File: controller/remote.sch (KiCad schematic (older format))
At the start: 24 parts, among them J1 Conn_01x03, J2 Conn_01x02, J3 Conn_01x07, J4 Conn_01x03, J5 Conn_01x03, J6 Conn_01x02, J7 Conn_01x03, U3 Arduino_Nano_v3.x, U4 AP1117, U5 nRF24L01+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

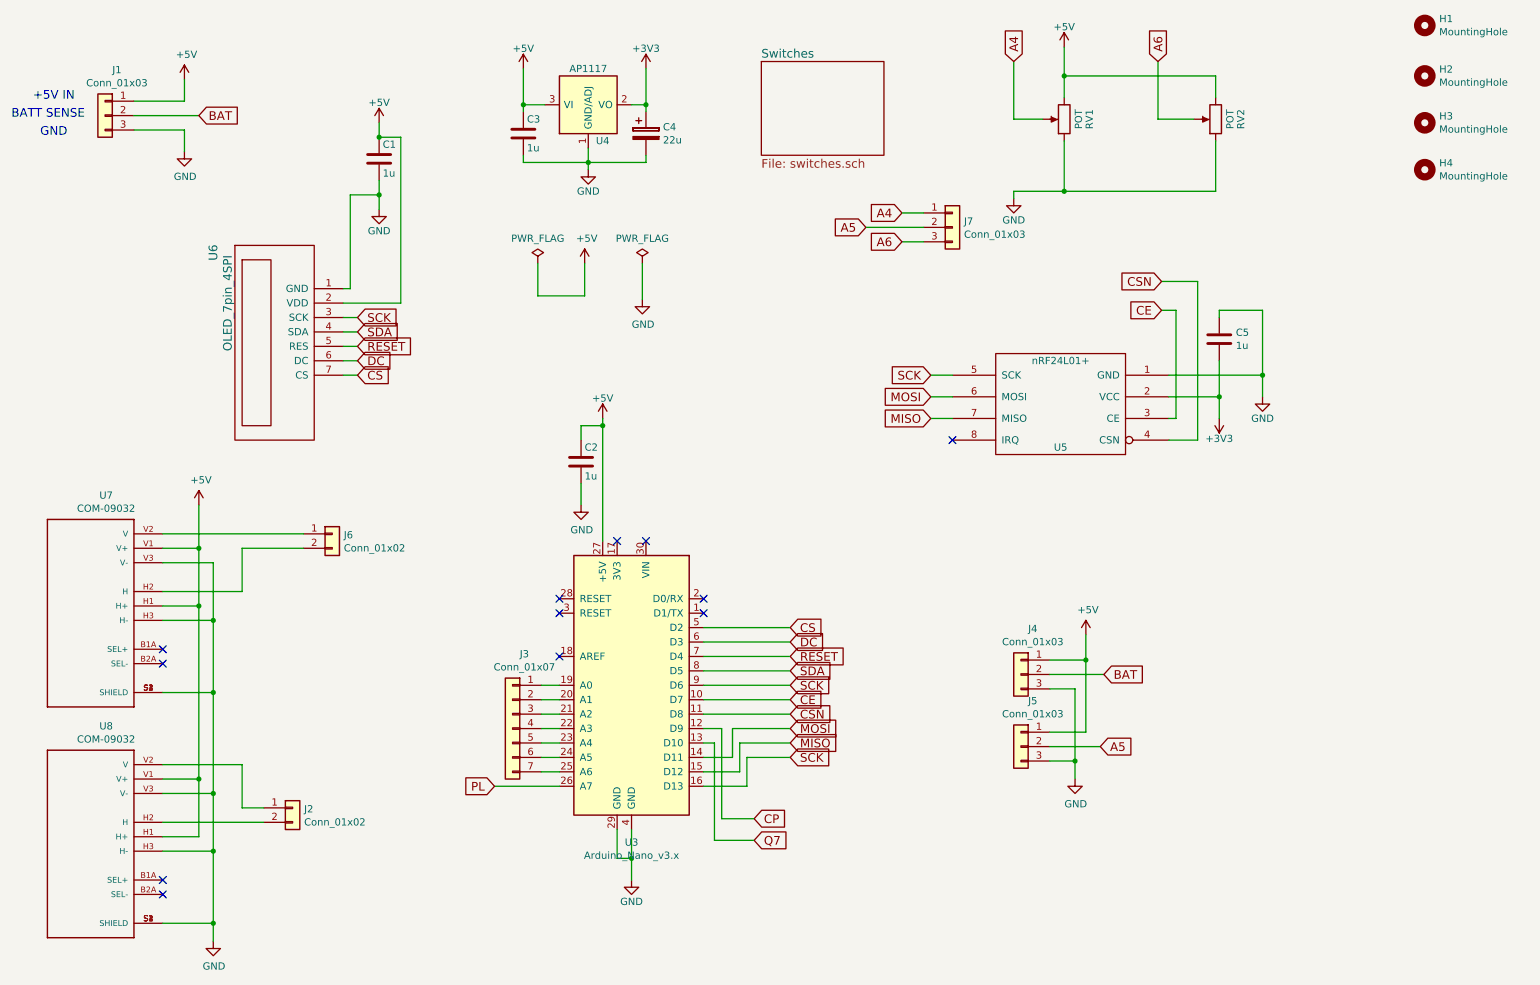
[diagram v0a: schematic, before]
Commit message: Update to 4-pin I2C display.
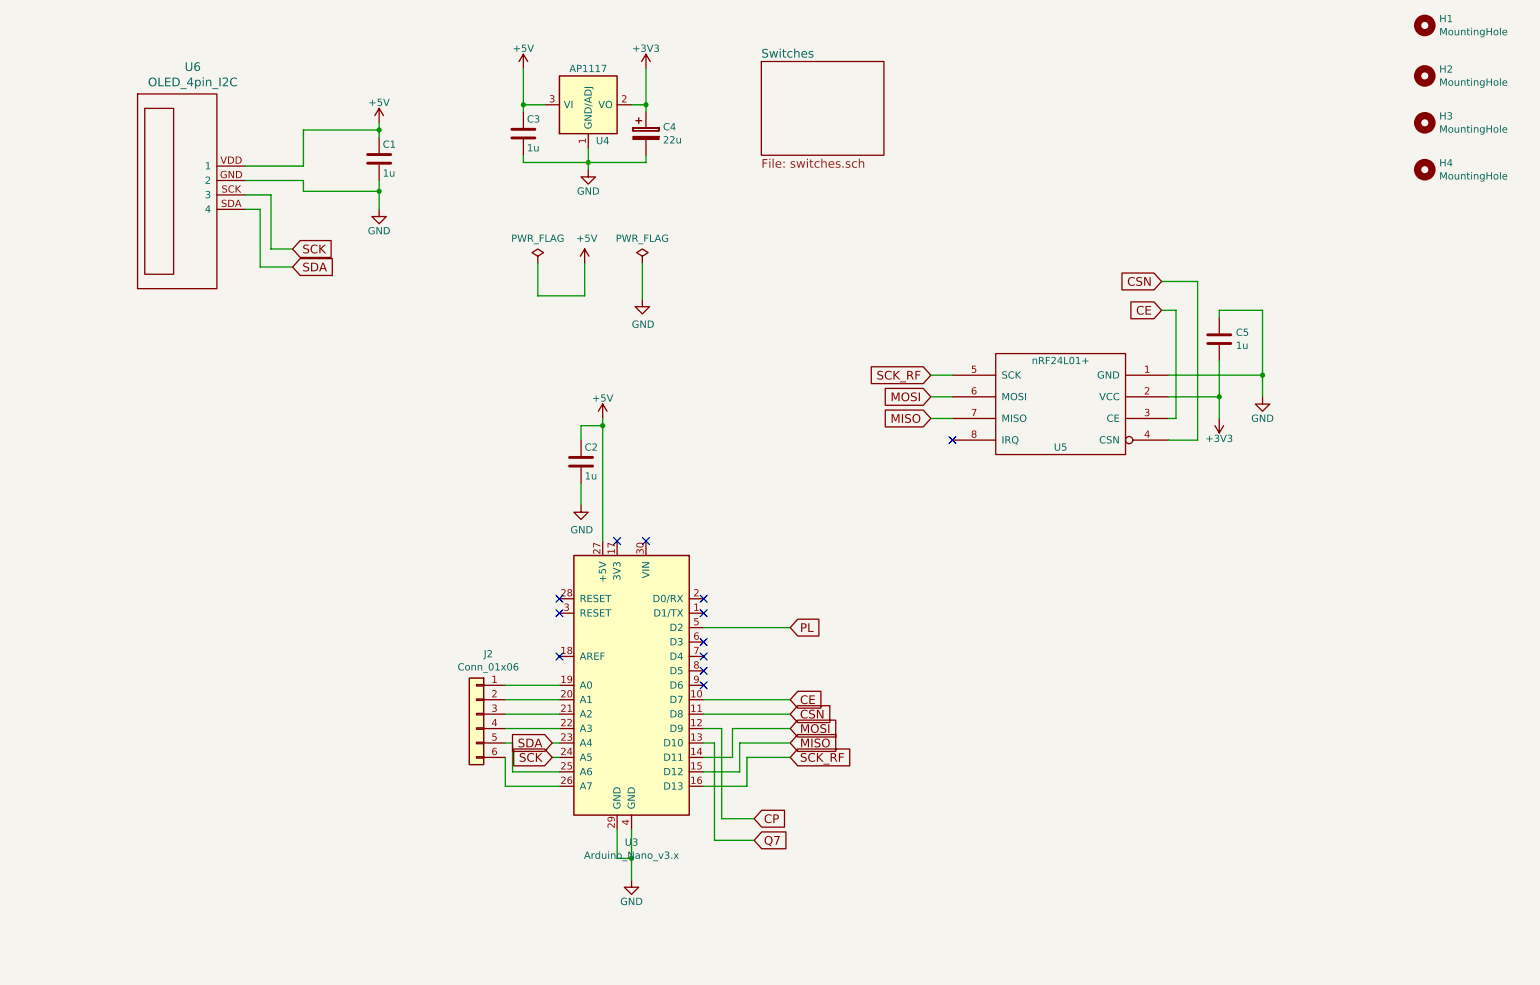
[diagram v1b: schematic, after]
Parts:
- removed J1, J4, J5, J7: Conn_01x03, Milling:JST_XH_B03B-XH-A_1x03_P2.50mm_Vertical_Milling, symbol Connector_Generic:Conn_01x03
- removed J2, J6: Conn_01x02, Milling:JST_XH_B02B-XH-A_1x02_P2.50mm_Vertical_Milling, symbol Connector_Generic:Conn_01x02
- removed J3: Conn_01x07, Connector_JST:JST_XH_B07B-XH-A_1x07_P2.50mm_Vertical, symbol Connector_Generic:Conn_01x07
- removed RV1, RV2: POT, Remote:Potentiometer_4mm_axis, symbol remote-rescue:POT
- removed U6: OLED_7pin_4SPI, Remote:Display_OLED_7pin_4SPI, symbol remote-rescue:OLED_7pin_4SPI
- removed U7, U8: COM-09032, Remote:XDCR_COM-09032, symbol COM-09032:COM-09032
- added J2: Conn_01x06, Connector_JST:JST_XH_B06B-XH-A_1x06_P2.50mm_Vertical, symbol Connector_Generic:Conn_01x06
- added U6: OLED_4pin_I2C, Remote:Display_OLED_4pin_I2C, symbol oled:OLED_4pin_I2C
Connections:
- net CS is gone; now on net PL: U3.5 (D2)
- net +5V: now also U6.VDD (1)
- net GND: now also U6.GND (2)
- net PL: no longer U3.26 (A7)
- net SCK: now also U3.24 (A5), U6.SCK (3); no longer U3.16 (D13), U3.9 (D6), U5.5 (SCK)
- net SDA: now also U3.23 (A4), U6.SDA (4); no longer U3.8 (D5)
- net at U3.19 (A0): now also J2.1 (Pin_1)
- net at U3.20 (A1): now also J2.2 (Pin_2)
- net at U3.21 (A2): now also J2.3 (Pin_3)
- net at U3.22 (A3): now also J2.4 (Pin_4)
- net at U3.25 (A6): now also J2.5 (Pin_5)
- net DC: no longer names the net of U3.6 (D3)
- net RESET: no longer names the net of U3.7 (D4)
- new net: J2.6 (Pin_6), U3.26 (A7)
- new net SCK_RF: U3.16 (D13), U5.5 (SCK)
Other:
- note removed: "+5V IN"
- note removed: "BATT SENSE"
- note removed: "GND"

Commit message: Update schematic.
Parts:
- added J1: Conn_01x02, Connector_JST:JST_XH_B02B-XH-A_1x02_P2.50mm_Vertical, symbol Connector_Generic:Conn_01x02
- added J3: Conn_01x04, Connector_JST:JST_XH_B04B-XH-A_1x04_P2.50mm_Vertical, symbol Connector_Generic:Conn_01x04
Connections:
- net +5V: now also J1.1 (Pin_1)
- net GND: now also J1.2 (Pin_2)
- net at U3.6 (D3): now also J3.1 (Pin_1)
- net at U3.7 (D4): now also J3.2 (Pin_2)
- net at U3.8 (D5): now also J3.3 (Pin_3)
- net at U3.9 (D6): now also J3.4 (Pin_4)
- no-connect marks 12 -> 8
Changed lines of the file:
@@
 Wire Wire Line
 	4300 5800 4250 5800
-NoConn ~ 5300 5100
-NoConn ~ 5300 5200
-NoConn ~ 5300 5300
-NoConn ~ 5300 5000
 Wire Wire Line
 	2125 2000 2225 2000
+$Comp
+L Connector_Generic:Conn_01x02 J1
+U 1 1 5E362610
+P 1325 3925
+F 0 "J1" H 1243 4142 50  0000 C CNN
+F 1 "Conn_01x02" H 1243 4051 50  0000 C CNN
+F 2 "Connector_JST:JST_XH_B02B-XH-A_1x02_P2.50mm_Vertical" H 1325 3925 50  0001 C CNN
+F 3 "~" H 1325 3925 50  0001 C CNN
+	1    1325 3925
+	-1   0    0    -1
+$EndComp
+$Comp
+L power:+5V #PWR01
+U 1 1 5E363020
+P 1800 3725
+F 0 "#PWR01" H 1800 3575 50  0001 C CNN
+F 1 "+5V" H 1815 3898 50  0000 C CNN
+F 2 "" H 1800 3725 50  0001 C CNN
+F 3 "" H 1800 3725 50  0001 C CNN
+	1    1800 3725
+	1    0    0    -1
+$EndComp
+$Comp
+L power:GND #PWR02
+U 1 1 5E3634FA
+P 1800 4225
+F 0 "#PWR02" H 1800 3975 50  0001 C CNN
+F 1 "GND" H 1805 4052 50  0000 C CNN
+F 2 "" H 1800 4225 50  0001 C CNN
+F 3 "" H 1800 4225 50  0001 C CNN
+	1    1800 4225
+	1    0    0    -1
+$EndComp
+Wire Wire Line
+	1525 4025 1800 4025
+Wire Wire Line
+	1800 4025 1800 4225
+Wire Wire Line
+	1525 3925 1800 3925
+Wire Wire Line
+	1800 3925 1800 3725
+$Comp
+L Connector_Generic:Conn_01x04 J3
+U 1 1 5E371548
+P 5650 5100
+F 0 "J3" H 5730 5092 50  0000 L CNN
+F 1 "Conn_01x04" H 5730 5001 50  0000 L CNN
+F 2 "Connector_JST:JST_XH_B04B-XH-A_1x04_P2.50mm_Vertical" H 5650 5100 50  0001 C CNN
+F 3 "~" H 5650 5100 50  0001 C CNN
+	1    5650 5100
+	1    0    0    -1
+$EndComp
+Wire Wire Line
+	5450 5000 5300 5000
+Wire Wire Line
+	5300 5100 5450 5100
+Wire Wire Line
+	5450 5200 5300 5200
+Wire Wire Line
+	5300 5300 5450 5300
 $EndSCHEMATC
